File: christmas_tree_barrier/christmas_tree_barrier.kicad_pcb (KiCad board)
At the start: 2 copper layers, 31 x 30.5 mm, 17 parts, among them CON1 AVR-ISP-6, IC1 MIC5225-3.3, J1 USB_OTG, J2 JSTPH, J3 JSTPH, Q1 Q_NPN_BEC, U1 ATTINY45-20SU, Y1 8Mhz

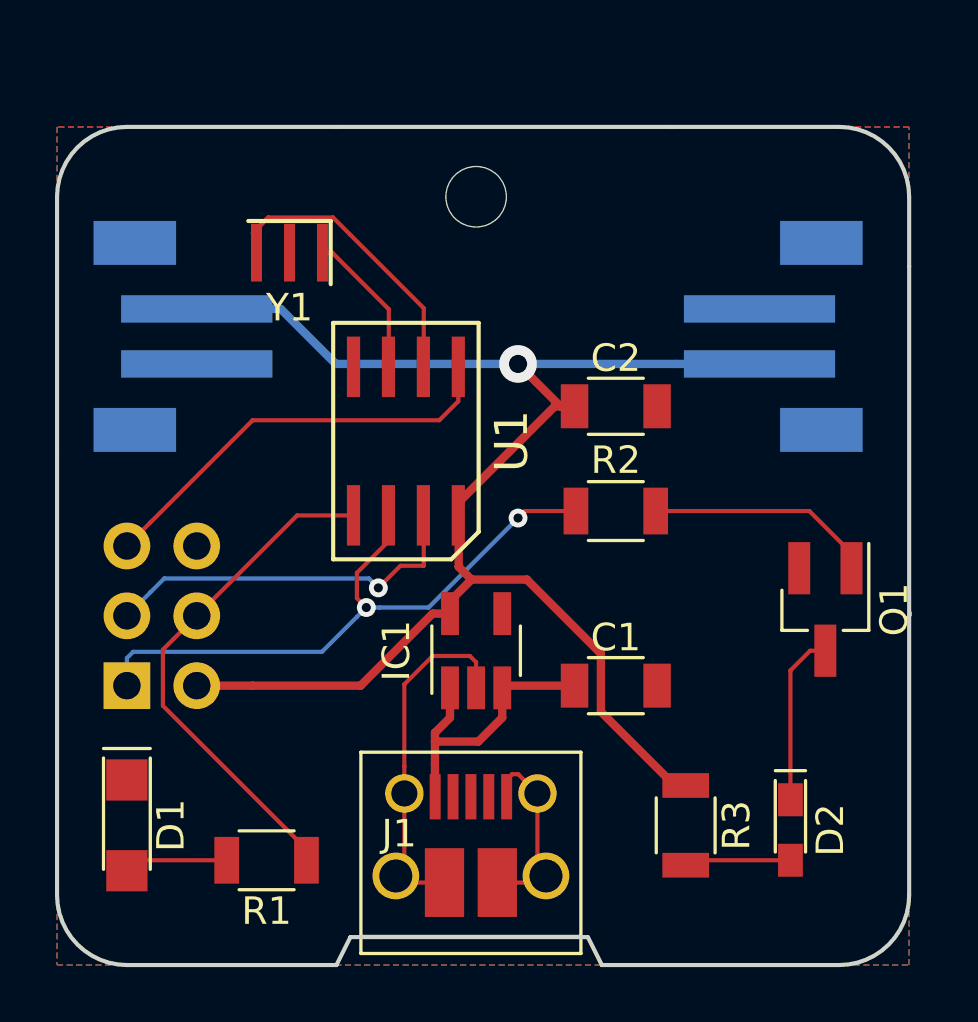
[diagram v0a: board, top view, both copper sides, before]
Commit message: Rev b of Christmas Tree Barrier
SOIC footprint is now fixed (wider pads)
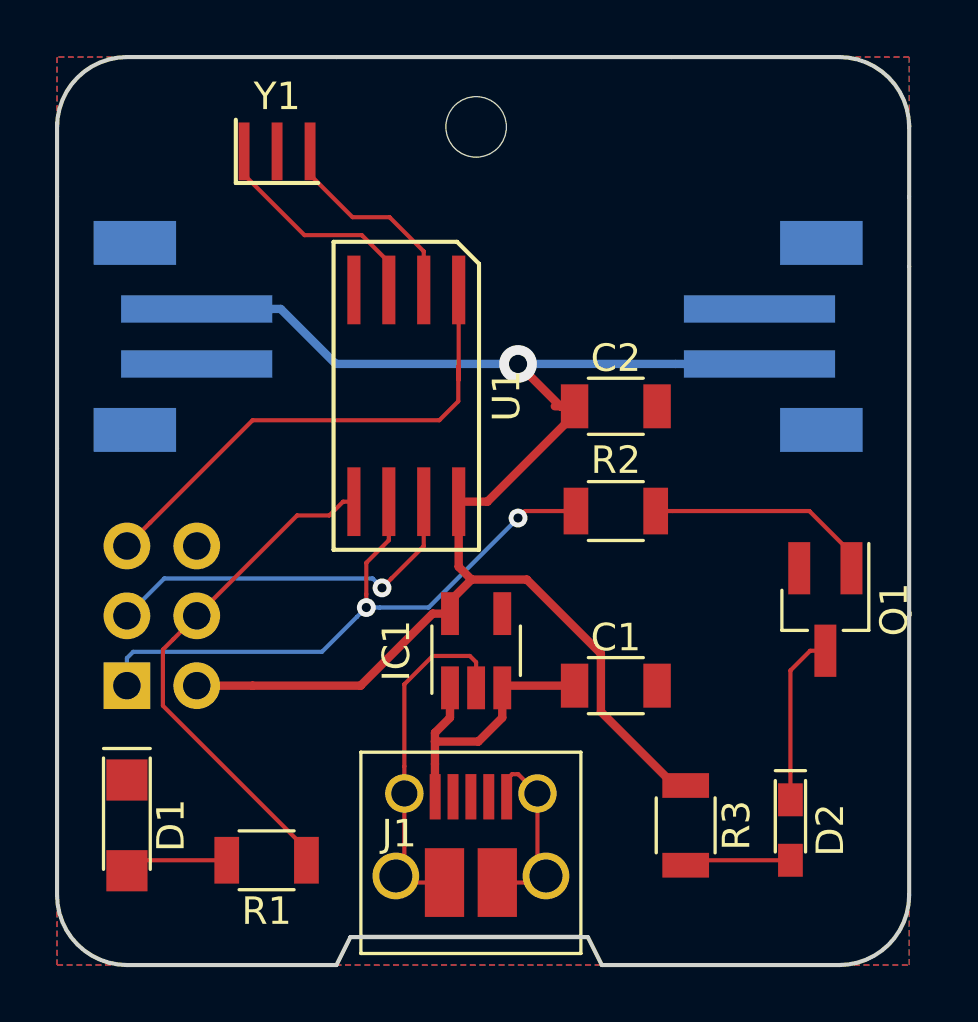
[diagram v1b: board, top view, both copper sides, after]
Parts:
- U1: footprint lib_fp:SOIC-8_5.35x5.40mm_Pitch1.27mm -> lib_fp:ATTINY-85-SOIC-8
- moved Y1 3.71 mm to (152.8, 105.0), turned to 0 degrees
- moved REF** 2.54 mm to (160.0, 104.1)
- moved U1 1.65 mm to (157.5, 113.9), turned to 180 degrees
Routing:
- net Net-(U1-Pad2): track 11.4 -> 7.54 mm
- net Net-(U1-Pad3): track 5.36 -> 8.44 mm
- net /RST: track 16.0 -> 18.8 mm
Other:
- board size 31 x 30.5 mm -> 31 x 33 mm
- board text added: "Roomba Christmas Tree Barrier (rev b) (C) Copyright 2017 Peter Dunshee @Petezah"
- board text removed: "Roomba Christmas Tree Barrier (C) Copyright 2017 Peter Dunshee @Petezah"
